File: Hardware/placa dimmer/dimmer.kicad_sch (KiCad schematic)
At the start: 60 parts, among them J1 Screw_Terminal_01x02, J2 Screw_Terminal_01x02, J3 Screw_Terminal_01x02, J4 Conn_01x05_Socket, Q1 2N7000, Q2 2N7000, Q4 NPN, Q6 NPN, U1 MOC3023M, U2 4N25, U3 CD40106, U4 MOC3023M

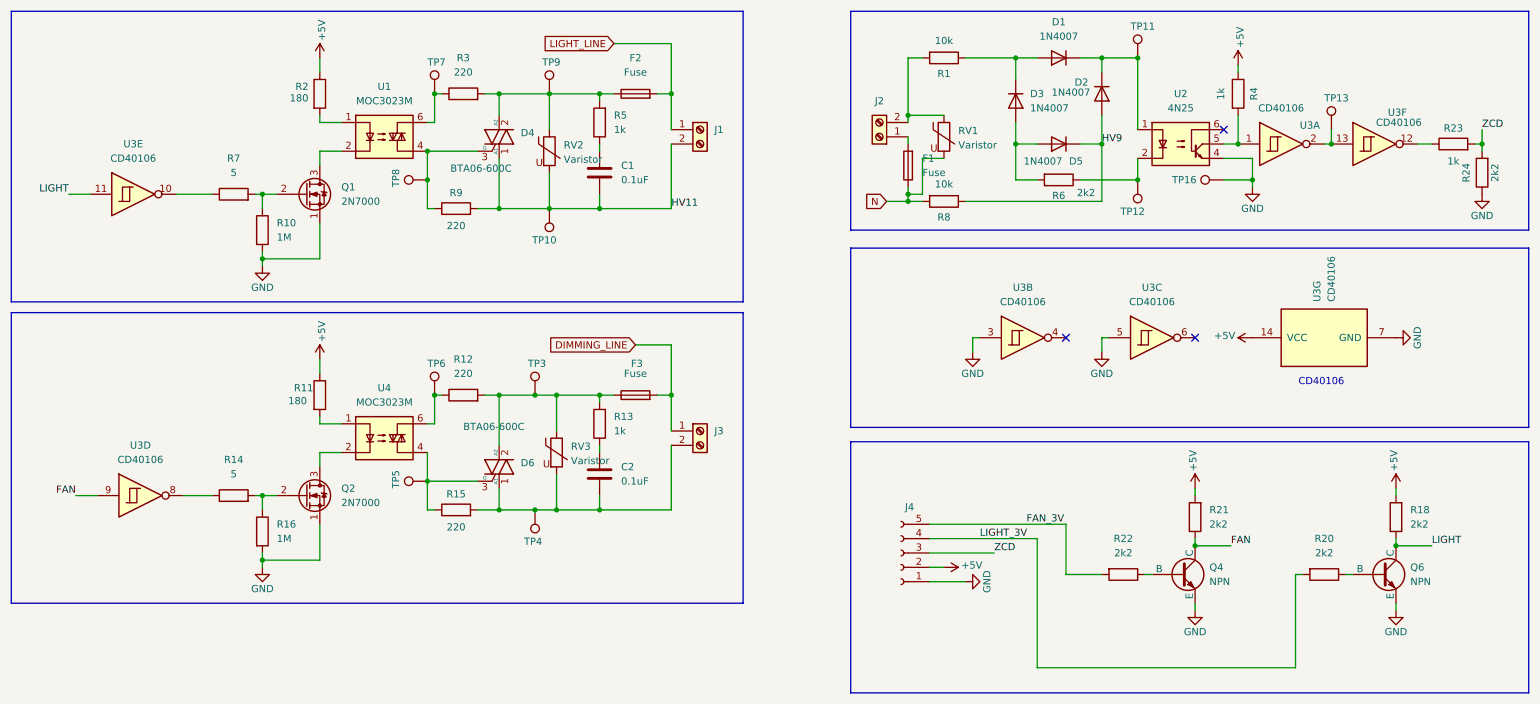
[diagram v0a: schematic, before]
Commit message: ajustes hardware
renombrar carpeta kicad -> hardware y anotaciones planos
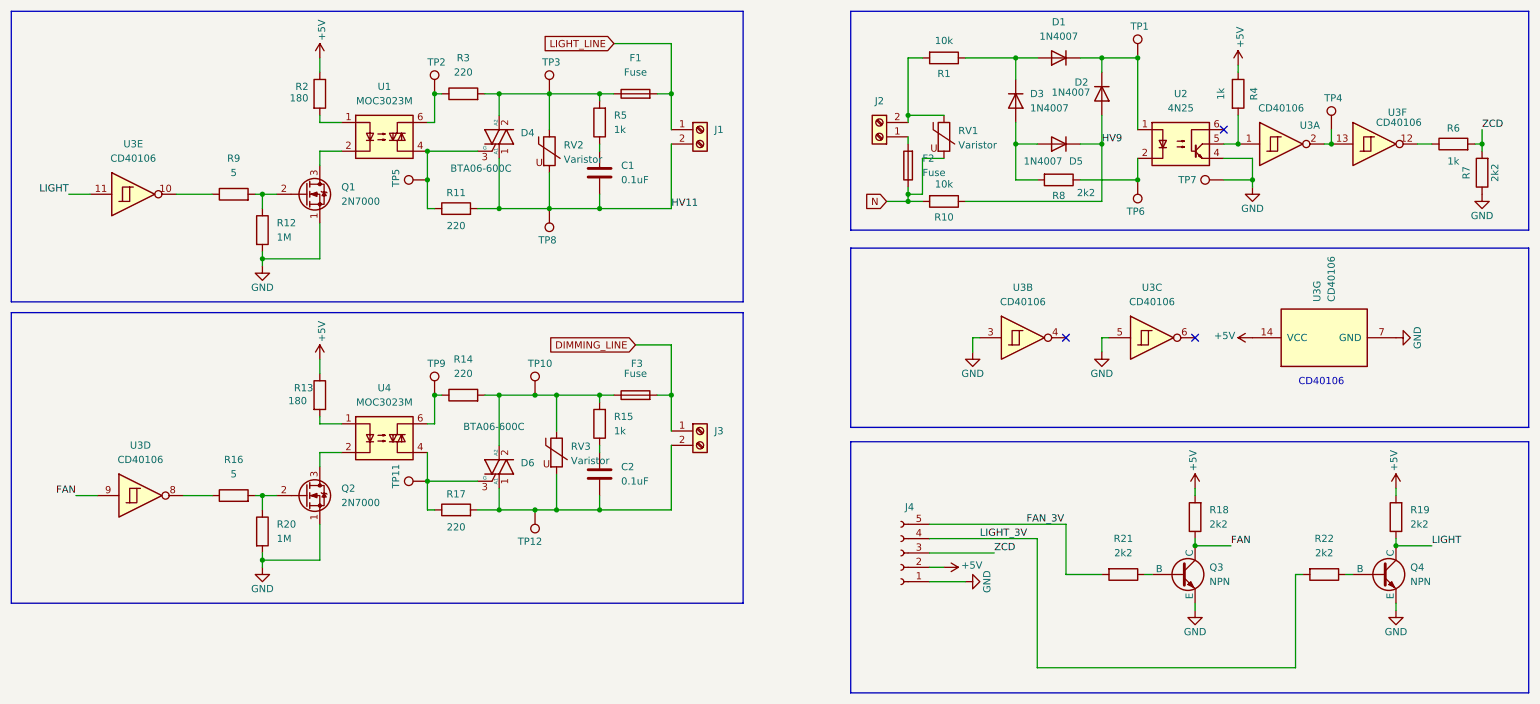
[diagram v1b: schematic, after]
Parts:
- renumbered F2 to F1, F1 to F2, Q4 to Q3, Q6 to Q4, R8 to R10, R9 to R11, R10 to R12, R11 to R13, R12 to R14, R13 to R15, R14 to R16, R15 to R17, R21 to R18, R18 to R19, R16 to R20, R22 to R21, R20 to R22, R23 to R6, R24 to R7, R6 to R8, R7 to R9, TP11 to TP1, TP3 to TP10, TP5 to TP11, TP4 to TP12, TP7 to TP2, TP9 to TP3, TP13 to TP4, TP8 to TP5, TP12 to TP6, TP16 to TP7, TP10 to TP8, TP6 to TP9
